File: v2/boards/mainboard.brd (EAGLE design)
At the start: 119.6 x 119.8 mm, 172 parts, among them IC1 LM2596S-ADJ, IC10 PCF8574P, IC11 UDN2981A, IC13 PAM8403, IC2 LM2596S-5.0, IC3 LD1117A, IC4 LM393, IC5 MCP101-300, IC6 TSOP34830, IC7 DRV8835, IC8 TEENSY 3.6, IC9 PCA9634, J1 Bat_In, J10 SPI_2, J11 I2C_0, J12 I2C_1, J13 I2C_3, J133 USB_Host, J14 BNO055, J15 Uart_2, J16 Uart_5, J17 Uart_6 (LP), J18 BPS, J19 Servo_2, J2 Erw_Pow, J20 Servo_3, J21 Erw_Servo, J22 Erw_PWM, J23 ESP01 Prog, J24 SWD, J25 SWD_KL02, J26 SWD_KL02, J27 SPEAKER_L, J28 SPEAKER_R, J29 AUDIO_TEENSY, J3 Servo_1, J30 Erw_ENA, J31 Erw_GPIO, J32 Erw_analog, J4 H-Bridge Mode, J5 I2C0_5V, J6 SPI_0, J7 SPI_0, J8 SPI_0, J9 SPI_2, SW1 TL32PO, U1 IRL3103, U2 BS108, U3 BS108, U4 BS108, U5 BS108, U6 BS108, U7 BS108, X1 max. 18V

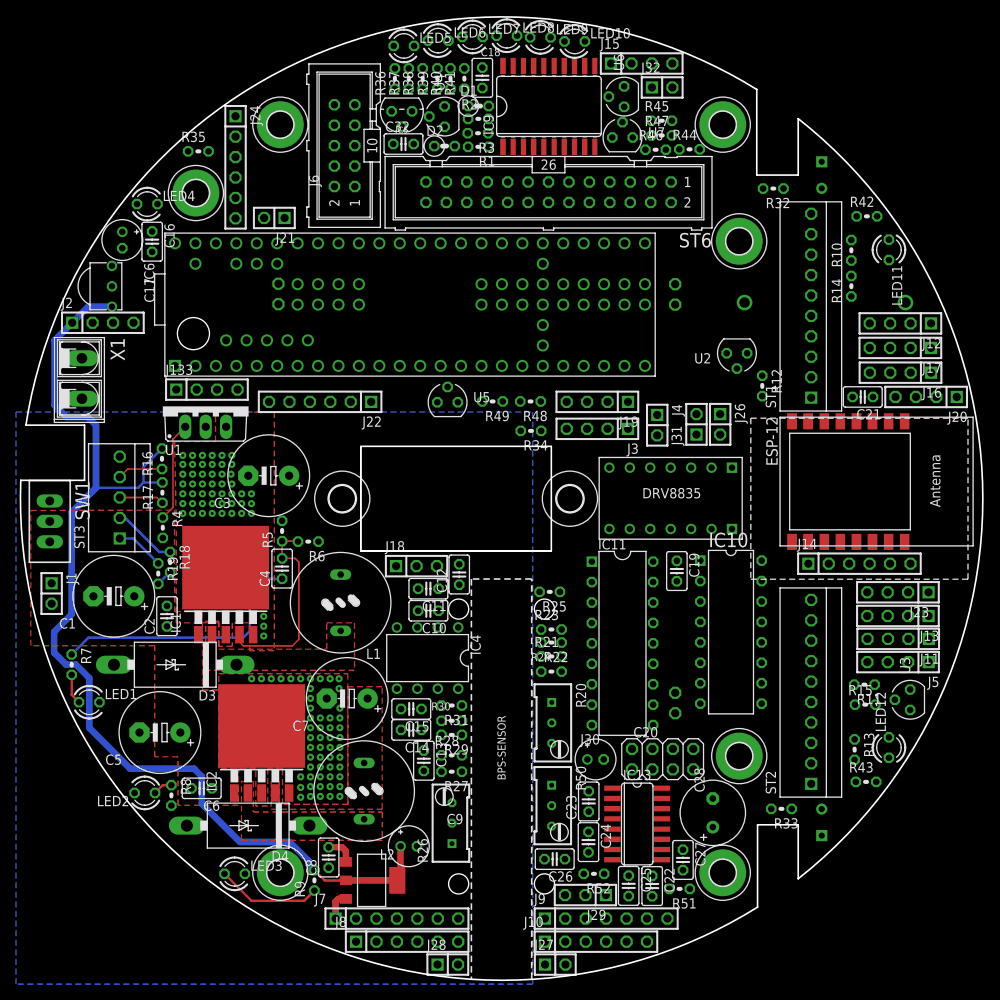
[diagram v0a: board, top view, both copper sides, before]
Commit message: ct-bot v2 schematic updated
 - use of i2c sensors
 - adjustable luminosity for CNY70 sensors
 - ENA driver circuit updated for low-side switching
 - ESP32 for Wi-Fi, SWD, RC5 decoding
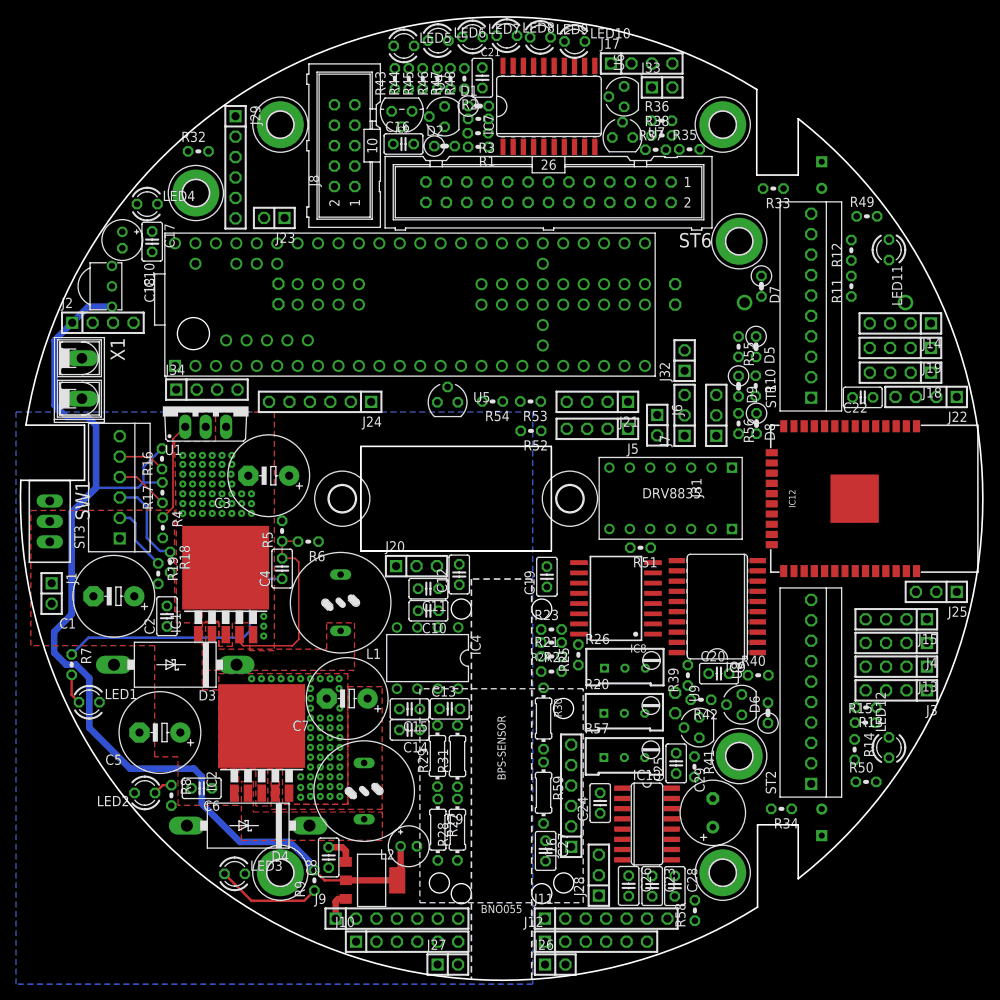
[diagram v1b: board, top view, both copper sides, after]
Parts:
- removed C32: 100nF, rcl:C025-025X050
- removed ESP-12: ESP-12, adafruit:ESP-12
- removed U2, U3: BS108, ct-bot:SOT54E
- added C29: 470uF, rcl:E3,5-8
- added D5, D6, D7, D8, D9: 1N4148, ct-bot:0207/2V
- added IC12: ESP-WROOM-32, ct-bot:ESP-WROOM-32
- added J33: Erw_analog, ct-bot:1X02
- added R53, R54: 4k7, rcl:0204V
- added R55, R56: 10k, rcl:0204V
- added R57: 5k, ct-bot:RTRIM64W
- added R58: ?, rcl:0204V
- added R59: ?, rcl:0204/7
- added U8, U9: BS108, ct-bot:SOT54E
- C17: value 220uF -> 100nF; device rcl:E2-5 -> rcl:C025-025X050
- C18: value 100nF -> 220uF; device rcl:C025-025X050 -> rcl:E2-5
- C20: value 100uF -> 100nF; device rcl:E2-5 -> rcl:C025-025X050
- C22: value 470nF -> 10uF
- C23, C27: value 1uF -> 470nF
- C25: value 100nF -> 1uF
- C26: value 470nF -> 100nF
- C28: value 470uF -> 1uF; device rcl:E3,5-8 -> rcl:C025-025X050
- IC10: value PCF8574P -> TSOP34830; device ct-bot:DIL16 -> ct-bot:TSOP348
- IC11: value UDN2981A -> DRV8835; device ct-bot:DIL18 -> ct-bot:DRV8835
- IC6: value TSOP34830 -> TEENSY 3.6; device ct-bot:TSOP348 -> ct-bot:T36
- IC7: value DRV8835 -> PCA9634; device ct-bot:DRV8835 -> ct-bot:SO20W
- IC8: value TEENSY 3.6 -> PCA9672; device ct-bot:T36 -> ct-bot:SO16W
- J10, J9: value SPI_2 -> SPI_0
- J11: value I2C_0 -> SPI_2; device ct-bot:1X04 -> ct-bot:1X07
- J12: value I2C_1 -> SPI_2; device ct-bot:1X04 -> ct-bot:1X06
- J13: value I2C_3 -> I2C_0
- J14: value BNO055 -> I2C_1; device ct-bot:1X06 -> ct-bot:1X04
- J15: value Uart_2 -> I2C_3
- J16: value Uart_5 -> BNO055; device ct-bot:1X04 -> ct-bot:1X06
- J17: value Uart_6 (LP) -> Uart_2
- J18: value BPS -> Uart_5; device ct-bot:1X03 -> ct-bot:1X04
- J19: value Servo_2 -> Uart_6 (LP)
- J20: value Servo_3 -> BPS; device ct-bot:1X04 -> ct-bot:1X03
- J21: value Erw_Servo -> Servo_2; device ct-bot:1X02 -> ct-bot:1X04
- J22: value Erw_PWM -> Servo_3; device ct-bot:1X06 -> ct-bot:1X04
- J23: value ESP01 Prog -> Erw_Servo; device ct-bot:1X04 -> ct-bot:1X02
- J24: value SWD -> Erw_PWM
- J25: value SWD_KL02 -> ESP32_PROG; device ct-bot:1X02/90 -> ct-bot:1X03
- J26: value SWD_KL02 -> SPEAKER_L
- J27: value SPEAKER_L -> SPEAKER_R
- J28: value SPEAKER_R -> AUDIO_TEENSY; device ct-bot:1X02 -> ct-bot:1X03
- J29: value AUDIO_TEENSY -> SWD; device ct-bot:1X03 -> ct-bot:1X06
- J3: value Servo_1 -> I2C0_5V
- J30: value Erw_ENA -> SWD_KL02; device pinhead:2X04 -> ct-bot:1X02/90
- J31: value Erw_GPIO -> Erw_ENA; device ct-bot:1X02 -> ct-bot:1X03
- J32: value Erw_analog -> Erw_GPIO
- J4: value H-Bridge Mode -> I2C3_5V; device ct-bot:1X02 -> ct-bot:1X04
- J5: value I2C0_5V -> Servo_1
- J6: value SPI_0 -> H-Bridge Mode; device con-harting-ml:ML10 -> ct-bot:1X02
- J7: value SPI_0 -> RC5_SEL; device ct-bot:1X07 -> ct-bot:1X03
- J8: device ct-bot:1X06 -> con-harting-ml:ML10
- LDR1, LDR2: value MPY54C569 -> (none)
- R10, R11: value 47k -> 180
- R12, R13: value 210 -> 47k
- R27, R28, R29, R30, R31: device rcl:0204V -> rcl:0204/7
- R32: value 470k -> 100
- R34: value 4k7 -> 470k
- R35: value 100 -> 4k7
- R37: value 3k9 -> 10k
- R38: value 220 -> 10k
- R39: value 590 -> 1k1
- R40: value 115 -> 1k1
- R42, R48: value 4k7 -> 1k8
- R44: value 4k7 -> 3k9
- R45: value 4k7 -> 220
- R46: value 10k -> 590
- R47: value 10k -> 115
- R50: value 5k -> 4k7; device ct-bot:RTRIM64W -> rcl:0204V
- R51: value ? -> 10k
- R52: value ? -> 4k7
- ST3: device ct-bot:TS_PS25_5 -> ct-bot:TS_PS25_6
- U1: device transistor-power:TO220BV -> ct-bot:TO220BV
- moved R43 105.2 mm to (-13.3, 52.2), turned to 90 degrees
- moved J29 100.4 mm to (-33.1, 41.2), turned to 270 degrees
- moved J8 99.3 mm to (-19.5, 43.9), turned to 90 degrees
- moved J25 93.3 mm to (54.1, -11.6), flipped to the top, turned to 180 degrees
- moved J23 90.4 mm to (-28.2, 34.9)
- moved R41 90.2 mm to (24.0, -33.3), turned to 270 degrees
- moved IC10 88.1 mm to (-48.4, 26.4)
- moved J12 85.7 mm to (11.7, -55.1), turned to 0 degrees
- moved R40 83.5 mm to (31.9, -21.9), turned to 0 degrees
- moved R39 80.4 mm to (23.2, -21.9)
- moved J30 77.5 mm to (-31.5, 25.5), flipped to the bottom, turned to 270 degrees
- moved R33 77.1 mm to (33.8, 38.6)
- moved J15 76.0 mm to (49.1, -15.0), turned to 180 degrees
- moved J22 75.3 mm to (52.8, 12.6)
- moved J7 72.1 mm to (22.8, 10.4), turned to 90 degrees
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- renumbered J133 to J34
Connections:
- removed net ABST_SHUT_L: IC10.7, U2.G
- removed net ABST_SHUT_R: IC10.9, U3.G
- removed net DRV_ERW_3: IC11.12, J30.6
- removed net DRV_ERW_4: IC11.11, J30.8
- removed net DRV_KANTLED: IC11.17, R14.2, R15.1
- removed net DRV_LINIE: IC11.16, R18.2, R19.2
- removed net DRV_RADLED: IC11.18, R12.2, R13.1
- removed net DRV_SCHRANKE: IC11.15, ST1.9
- removed net ENA_ERW_2: IC10.12, IC11.6, J30.3
- removed net ENA_ERW_3: IC11.8, J30.5
- removed net ENA_ERW_4: IC11.7, J30.7
- removed net ENA_KANTLED: IC10.5, IC11.2
- removed net ENA_LINIE: IC10.6, IC11.3
- removed net ENA_RADLED: IC10.4, IC11.1
- removed net ENA_SCHRANKE: IC10.10, IC11.4
- removed net N$12: ESP-12.10, J23.3
- removed net N$14: ESP-12.12, J23.2
- new net ABST_SHDN_L: D5.2, IC8.4
- new net ABST_SHDN_R: D6.2, IC8.5
- new net BNO055_RESET: IC8.7, J16.6
- new net DRV_KANTLED_L: IC9.8, R11.2
- new net DRV_KANTLED_R: IC9.9, R15.1
- new net DRV_LINE_L: IC9.11, R19.2
- new net DRV_LINE_R: IC9.12, R18.2
- new net DRV_RADLED_L: IC9.6, R10.2
- new net DRV_RADLED_R: IC9.7, R14.1
- new net EN: D8.1, IC12.3, R56.1
- new net ENA_AUDIO: IC13.12, IC8.9
- new net ESP32_PROG: D9.2, IC8.11
- new net ESP32_RESET: D8.2, IC8.10
- new net GPIO_28: IC6.28, J7.3
- new net IO0: D9.1, IC12.25, R55.2
- new net IO10: IC12.18
- new net IO11: IC12.19
- new net IO13: IC12.16
- new net IO15: IC12.23
- new net IO18: IC12.30
- new net IO19: IC12.31
- new net IO21: IC12.33
- new net IO34: IC12.6
- new net IO35: IC12.7
- new net IO36: IC12.4
- new net IO39: IC12.5
- new net IO4: IC12.26
- new net IO5: IC12.29
- new net IO6: IC12.20
- new net IO7: IC12.21
- new net IO8: IC12.22
- new net IO9: IC12.17
- new net N$49: IC8.3, R51.1
- new net RC5_ESP32: IC12.37, J7.1
- new net RXD0: IC12.34, J25.3
- new net SCHRANKE_SHDN: D7.2, IC8.6
- new net SCL3_5V: IC7.18, IC8.14, IC9.18, J4.4, R42.1, U8.D
- new net SDA3_5V: IC7.19, IC8.15, IC9.19, J4.3, R41.1, U9.D
- new net TXD0: IC12.35, J25.2
- new net VL6180X_SHDN: D7.1, ST1.5
- net +3V3: now also C22.1, IC10.3, IC12.2, J20.3, J8.10, R12.2, R13.1, R36.2, R39.2, R40.2, R52.2, R53.2, R54.2, R55.1, R56.2, U8.G, U9.G; no longer C21.1, ESP-12.3, ESP-12.8, IC6.3, J18.3, J23.1, J6.10, R10.2, R11.1, R44.2, R45.2, R48.2, R49.2
- net +5V: now also C17.1, C18.+, C20.1, C21.1, C25.1, C28.1, C29.+, IC11.VCC, IC6.VIN, IC7.1, IC7.20, IC7.3, IC7.5, IC8.16, IC9.4, J10.1, J14.2, J16.1, J18.2, J19.2, J3.2, J4.2, J9.1, R37.2, R38.2, R41.2, R42.2, R44.1, R45.1, R46.1, R47.1, R48.1, R49.1, R50.1, R51.2, ST1.1, ST2.1, ST3.1; no longer C16.1, C17.+, C18.1, C20.+, C23.1, C27.1, C28.+, IC10.1, IC10.16, IC11.9, IC7.VCC, IC8.VIN, J10.2, J14.1, J16.2, J4.1, J5.2, J7.1, J9.2, R36.1, R37.1, R38.1, R39.1, R40.1, R41.1, R42.1, R46.2, R47.2, ST1.3, ST2.3
- net +6V: now also IC11.VIN, J21.2, J22.2, J5.2; no longer IC7.VIN, J19.2, J20.2, J3.2
- net 3V3_TEENSY: now also C16.1, IC6.3V3(1), IC6.3V3(2), IC6.3V3(3), IC6.3V3(4), J29.1; no longer C32.1, IC8.3V3(1), IC8.3V3(2), IC8.3V3(3), IC8.3V3(4), J24.1
- net A22_DAC1: now also IC6.DAC1, J33.1; no longer IC8.DAC1, J32.1
- net AUDIO_OUT: now also IC6.DAC0, J28.1, J33.2; no longer IC8.DAC0, J29.1, J32.2
- net BAT_IN_FB: now also IC6.39; no longer IC8.39
- net BPS: now also IC6.42, J20.1; no longer IC8.42, J18.1
- net DRV_ERW_1: now also IC9.13, J31.2; no longer IC11.14, J30.2
- net DRV_ERW_2: now also IC9.14, J31.3; no longer IC11.13, J30.4
- net ENA_ERW_1: now also IC8.12, J31.1; no longer IC10.11, IC11.5, J30.1
- net ENC_L: now also ST1.8; no longer ST1.1
- net ENC_R: now also ST2.8; no longer ST2.1
- net FERNBED: now also IC10.1, J7.2; no longer IC6.1, IC8.28
- net GND: now also C17.2, C18.-, C20.2, C22.2, C26.2, C28.2, C29.-, IC11.LGND, IC11.MGND, IC12.1, IC12.15, IC12.24, IC12.38, IC6.AGND, IC6.G0, IC6.G1, IC6.G2, IC6.G3, IC6.G4, IC6.G5, IC6.G6, IC7.10, IC7.15, IC7.16, IC7.17, IC7.2, IC7.4, IC8.1, IC8.2, IC8.8, J10.2, J14.1, J16.3, J18.1, J20.2, J21.1, J22.1, J25.1, J29.3, J4.1, J9.2, R57.3, ST3.6; no longer C17.-, C18.2, C20.-, C23.2, C27.2, C28.-, C32.2, ESP-12.9, IC10.3, IC10.8, IC11.10, IC6.2, IC7.LGND, IC7.MGND, IC8.AGND, IC8.G0, IC8.G1, IC8.G2, IC8.G3, IC8.G4, IC8.G5, IC8.G6, IC9.4, J10.1, J14.3, J16.1, J18.2, J20.1, J23.4, J24.3, J6.2, J7.2, J9.1, R50.3, ST3.5, U2.S, U3.S
- net GPIO_24: now also IC6.24, J32.1; no longer IC8.24, J31.1
- net GPIO_46: now also IC6.46, J32.2; no longer IC8.46, J31.2
- net KANTE_L: now also IC6.18, R12.1, ST1.9; no longer IC8.18, R10.1, ST1.6
- net KANTE_R: now also IC6.19, R13.2, ST2.9; no longer IC8.19, R11.2, ST2.6
- net KL02_DC: now also IC12.14, J30.1; no longer J25.1, J26.1
- net KL02_DD: now also IC12.13, J30.2; no longer J25.2, J26.2
- net LDR_L: now also IC6.49, R33.1; no longer IC8.49, R32.1
- net LDR_R: now also IC6.50, R34.1; no longer IC8.50, R33.1
- net LINE_IN_L: now also J28.2, R57.1; no longer J29.2, R50.1
- net LINE_IN_R: now also C27.2, J28.3; no longer C26.2, J29.3
- net LINIE_L: now also IC6.A10, ST3.4; no longer IC8.A10, ST3.3
- net LINIE_R: now also IC6.A11, ST3.5; no longer IC8.A11, ST3.4
- net MOT_L_1: now also IC11.AOUT1; no longer IC7.AOUT1
- net MOT_L_2: now also IC11.AOUT2; no longer IC7.AOUT2
- net MOT_L_DIR: now also IC11.APHASE, IC6.40; no longer IC7.APHASE, IC8.40
- net MOT_L_PWM: now also IC11.AENBL, IC6.35; no longer IC7.AENBL, IC8.35
- net MOT_R_1: now also IC11.BOUT1; no longer IC7.BOUT1
- net MOT_R_2: now also IC11.BOUT2; no longer IC7.BOUT2
- net MOT_R_DIR: now also IC11.BPHASE, IC6.41; no longer IC7.BPHASE, IC8.41
- net MOT_R_PWM: now also IC11.BENBL, IC6.36; no longer IC7.BENBL, IC8.36
- net N$1: now also ST3.3; no longer ST3.2
- net N$13: now also IC7.8; no longer IC9.8
- net N$15: now also IC7.9; no longer IC9.9
- net N$16: now also IC7.11; no longer IC9.11
- net N$17: now also IC7.12; no longer IC9.12
- net N$18: now also IC7.13; no longer IC9.13
- net N$19: now also IC7.14; no longer IC9.14
- net N$20: now also R43.2; no longer R36.2
- net N$21: now also R44.2; no longer R37.2
- net N$22: now also R45.2; no longer R38.2
- net N$23: now also R46.2; no longer R39.2
- net N$24: now also R47.2; no longer R40.2
- net N$25: now also R48.2; no longer R41.2
- net N$26: now also R49.2; no longer R42.2
- net N$27: now also R50.2; no longer R43.2
- net N$28: now also R32.1; no longer R35.1
- net N$3: now also IC11.MODE, J6.2; no longer IC7.MODE, J4.2
- net N$30: now also ST3.2; no longer ST3.1
- net N$31: now also J26.2; no longer J27.2
- net N$32: now also J26.1; no longer J27.1
- net N$33: now also C26.1; no longer C25.1
- net N$40: now also R58.1; no longer R51.1
- net N$41: now also C23.1, R58.2; no longer C22.1, R51.2
- net N$42: now also C23.2, R57.2; no longer C22.2, R50.2
- net N$43: now also J27.1; no longer J28.1
- net N$44: now also J27.2; no longer J28.2
- net N$45: now also R14.2, ST2.6; no longer R13.2, ST2.2
- net N$46: now also R59.1; no longer R52.1
- net N$47: now also R10.1, ST1.6; no longer R12.1, ST1.2
- net N$48: now also C27.1, R59.2; no longer C26.1, R52.2
- net N$51: now also R11.1, ST1.7; no longer R14.1, ST1.5
- net N$53: now also ST2.7; no longer ST2.5
- net N$6: now also IC7.6; no longer IC9.6
- net N$7: now also IC7.7; no longer IC9.7
- net PWM_ERW_1: now also IC6.16, J24.1; no longer IC8.16, J22.1
- net PWM_ERW_2: now also IC6.17, J24.2; no longer IC8.17, J22.2
- net PWM_ERW_3: now also IC6.30, J24.3, J8.9; no longer IC8.30, J22.3, J6.9
- net PWM_ERW_4: now also IC6.29, J24.4; no longer IC8.29, J22.4
- net PWM_ERW_5: now also IC6.4, J24.5; no longer IC8.4, J22.5
- net PWM_ERW_6: now also IC6.3, J24.6; no longer IC8.3, J22.6
- net RAD_L: now also IC6.43; no longer IC8.43
- net RAD_R: now also IC6.44; no longer IC8.44
- net RESET: now also IC12.36, IC6.R, J29.2; no longer IC8.R, J24.2
- net RX1: now also IC6.27; no longer IC8.27
- net RX2: now also IC6.9, J17.4; no longer IC8.9, J15.4
- net RX5: now also IC12.28, IC6.34, J18.4; no longer ESP-12.16, IC8.34, J16.4
- net RX6: now also IC6.47, J19.4; no longer IC8.47, J17.4
- net SCL0: now also IC6.7, J13.4, R36.1; no longer IC10.14, IC8.7, IC9.18, J11.4, R45.1
- net SCL0_5V: now also J16.5, J3.4, R38.1, ST1.3, ST2.3; no longer J14.5, J5.4, R47.1, ST1.8, ST2.8
- net SCL1: now also IC6.37, J14.4; no longer IC8.37, J12.4
- net SCL3: now also IC12.11, IC6.57, J15.3, R40.1, U8.S; no longer IC8.57, J13.3
- net SDA0: now also IC6.8, J13.3, R35.1; no longer IC10.15, IC8.8, IC9.19, J11.3, R44.1
- net SDA0_5V: now also J16.4, J3.3, R37.1, ST1.2, ST2.2; no longer J14.4, J5.3, R46.1, ST1.7, ST2.7
- net SDA1: now also IC6.38, J14.3; no longer IC8.38, J12.3
- net SDA3: now also IC12.10, IC6.56, J15.4, R39.1, U9.S; no longer IC8.56, J13.4
- net SERVO1_FB: now also IC6.22, J5.4; no longer IC8.22, J3.4
- net SERVO1_PWM: now also IC6.5, J5.3, R52.1; no longer IC8.5, J3.3, R34.1
- net SERVO2_FB: now also IC6.23, J21.4; no longer IC8.23, J19.4
- net SERVO2_PWM: now also IC6.6, J21.3, R53.1; no longer IC8.6, J19.3, R48.1
- net SERVO3_PWM: now also IC6.25, J22.3, R54.1; no longer IC8.25, J20.3, R49.1
- net SERVO4_PWM: now also IC6.20, J23.1, J9.6; no longer IC8.20, J21.1, J7.6
- net SERVO5_PWM: now also IC6.21, J10.6, J23.2, J9.7; no longer IC8.21, J21.2, J7.7, J8.6
- net SPI0_CS0: now also IC6.2, J8.6; no longer IC8.2, J6.6
- net SPI0_CS4: now also IC6.15, J8.7; no longer IC8.15, J6.7
- net SPI0_CS5: now also IC6.45, J8.8; no longer IC8.45, J6.8
- net SPI0_MISO: now also IC6.12, J10.4, J9.4; no longer IC8.12, J6.4, J7.4
- net SPI0_MOSI: now also IC6.11, J10.3, J9.3; no longer IC8.11, J6.3, J7.3
- net SPI0_SCK: now also IC6.14, J10.5, J9.5; no longer IC8.14, J6.5, J7.5
- net SPI1_CS0: now also IC6.31; no longer IC8.31
- net SPI1_MISO: now also IC6.1; no longer IC8.1
- net SPI1_MOSI: now also IC6.0; no longer IC8.0
- net SPI1_SCK: now also IC6.32; no longer IC8.32
- net SPI2_CS0: now also IC6.55, J11.6; no longer IC8.55, J9.6
- net SPI2_CS1: now also IC6.54, J11.7, J12.6; no longer IC8.54, J10.6, J9.7
- net SPI2_MISO: now also IC6.51, J11.4, J12.4; no longer IC8.51, J10.4, J9.4
- net SPI2_MOSI: now also IC6.52, J11.3, J12.3; no longer IC8.52, J10.3, J9.3
- net SPI2_SCK: now also IC6.53, J11.5, J12.5; no longer IC8.53, J10.5, J9.5
- net SWCLK: now also IC12.9, IC6.DC, J29.5; no longer IC8.DC, J24.5
- net SWDIO: now also IC12.8, IC6.DD, J29.6; no longer IC8.DD, J24.6
- net SWD_EN: now also IC12.12, IC6.DE, J29.4; no longer IC8.DE, J24.4
- net TEENSY_LED: now also IC6.13; no longer IC8.13
- net TX1: now also IC6.26; no longer IC8.26
- net TX2: now also IC6.10, J17.3; no longer IC8.10, J15.3
- net TX5: now also IC12.27, IC6.33, J18.3; no longer ESP-12.15, IC8.33, J16.3
- net TX6: now also IC6.48, J19.3; no longer IC8.48, J17.3
- net USB1_D+: now also IC6.D+; no longer IC8.D+
- net USB1_D-: now also IC6.D-; no longer IC8.D-
- net VBAT_RTC: now also IC6.VBAT; no longer IC8.VBAT
- net VL53L0X_SHUT_L: now also D5.1; no longer U2.D
- net VL53L0X_SHUT_R: now also D6.1; no longer U3.D
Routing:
- net N$1: track 8.01 -> 11.3 mm
- net N$30: track 6.07 -> 8.38 mm
- net DRV_LINIE: track 2.07 -> 0.00 mm
- net LINIE_L: track 5.58 -> 6.63 mm
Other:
- board text added: "BNO055"

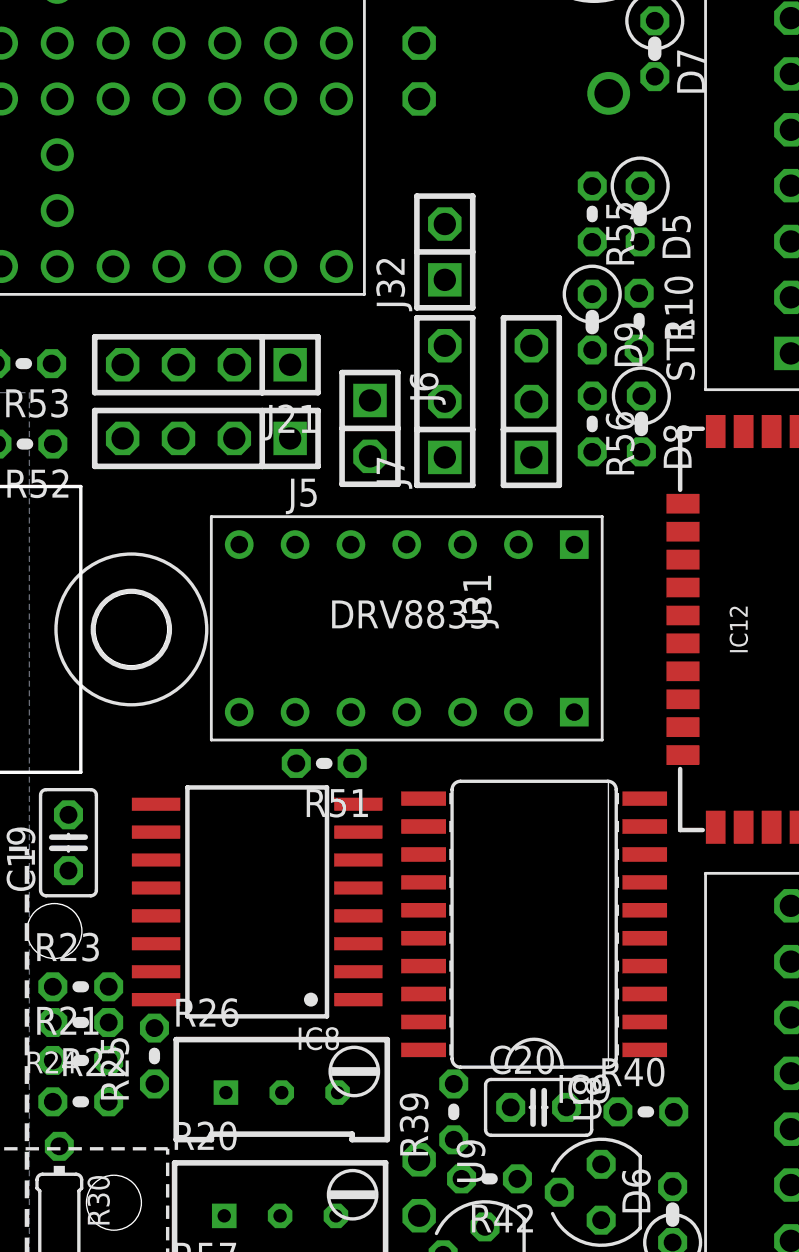
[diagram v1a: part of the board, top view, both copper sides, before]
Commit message: PCA9672D (no longer manufactured) replaced with PCA9554D
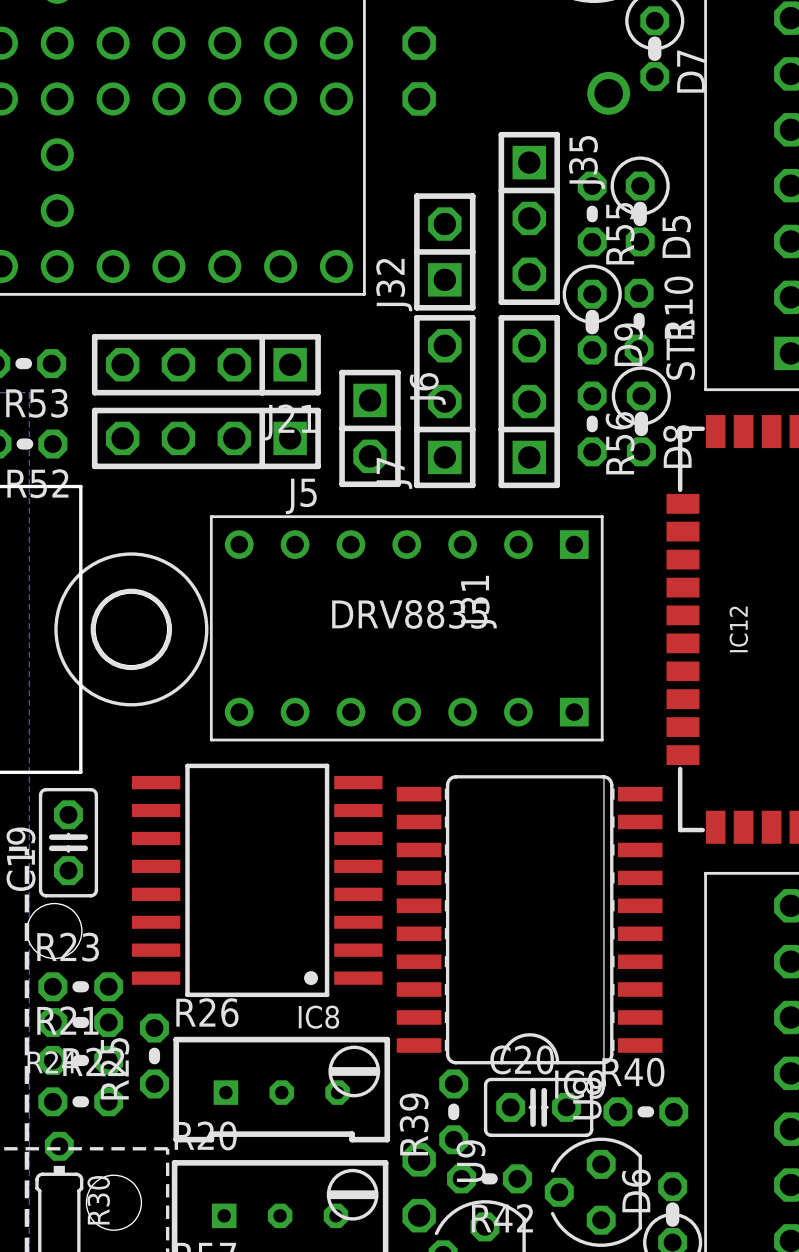
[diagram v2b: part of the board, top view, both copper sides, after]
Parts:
- removed R51: 10k, rcl:0204V
- added J35: ESP32_PROG, ct-bot:1X03
- IC8: value PCA9672 -> PCA9554
- J25: value ESP32_PROG -> ESP32_Uart
- moved IC8 0.98 mm to (14.2, -11.4)
- moved IC9 0.29 mm to (26.6, -13.2)
- moved J31 0.10 mm to (26.6, 10.4)
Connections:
- removed net N$49: IC8.3, R51.1
- net +5V: no longer R51.2
- net ESP32_PROG: now also J35.2
- net ESP32_RESET: now also J35.3
- net GND: now also IC8.3, J35.1
- net SCL0_5V: now also IC8.14
- net SCL3_5V: no longer IC8.14
- net SDA0_5V: now also IC8.15
- net SDA3_5V: no longer IC8.15

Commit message: resistor values for audio amp updated
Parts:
- R58, R59: value ? -> 10k
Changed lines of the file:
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@@
 <attribute name="VALUE" x="-24.9682" y="-6.1468" size="1.27" layer="27" ratio="10" rot="R90"/>
 </element>
-<element name="R58" library="rcl" library_urn="urn:adsk.eagle:library:334" package="0204V" package3d_urn="urn:adsk.eagle:package:23495/1" value="?" x="24.0356" y="-51.188878125" smashed="yes" rot="R90">
+<element name="R58" library="rcl" library_urn="urn:adsk.eagle:library:334" package="0204V" package3d_urn="urn:adsk.eagle:package:23495/1" value="10k" x="24.0356" y="-51.188878125" smashed="yes" rot="R90">
 <attribute name="NAME" x="22.8672" y="-53.322478125" size="1.27" layer="25" ratio="10" rot="R90"/>
 <attribute name="SPICEPREFIX" value="R" x="151.0356" y="77.081121875" size="1.778" layer="27" rot="R90" display="off"/>
@@
 <attribute name="VALUE" x="-9.2202" y="-61.087" size="1.27" layer="27"/>
 </element>
-<element name="R59" library="rcl" library_urn="urn:adsk.eagle:library:334" package="0204/7" package3d_urn="urn:adsk.eagle:package:23498/2" value="?" x="5.2226375" y="-36.56024375" smashed="yes" rot="R270">
+<element name="R59" library="rcl" library_urn="urn:adsk.eagle:library:334" package="0204/7" package3d_urn="urn:adsk.eagle:package:23498/2" value="10k" x="5.2226375" y="-36.56024375" smashed="yes" rot="R270">
 <attribute name="NAME" x="6.3910375" y="-34.42664375" size="1.27" layer="25" ratio="10" rot="R270"/>
 <attribute name="SPICEPREFIX" value="R" x="5.2226375" y="-36.56024375" size="1.778" layer="27" rot="R270" display="off"/>
